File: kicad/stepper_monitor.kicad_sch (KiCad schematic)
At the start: 59 parts, among them J1 Conn_01x04_Pin, J2 Conn_01x04_Pin, J3 Conn_01x02_Pin, J4 USB_C_Receptacle_USB2.0, J5 JTAG, M1 Motor-simple_stepper_motor_an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, Q1 MMDT2222A, SW1 SW_Push, U1 5V, U2 CP2102N-A01-GQFN28, U3 AMS1117-3.3, U4 CC6920BSO-5A, U5 CC6920BSO-5A, U6 ESP32-WROOM-32U-N4

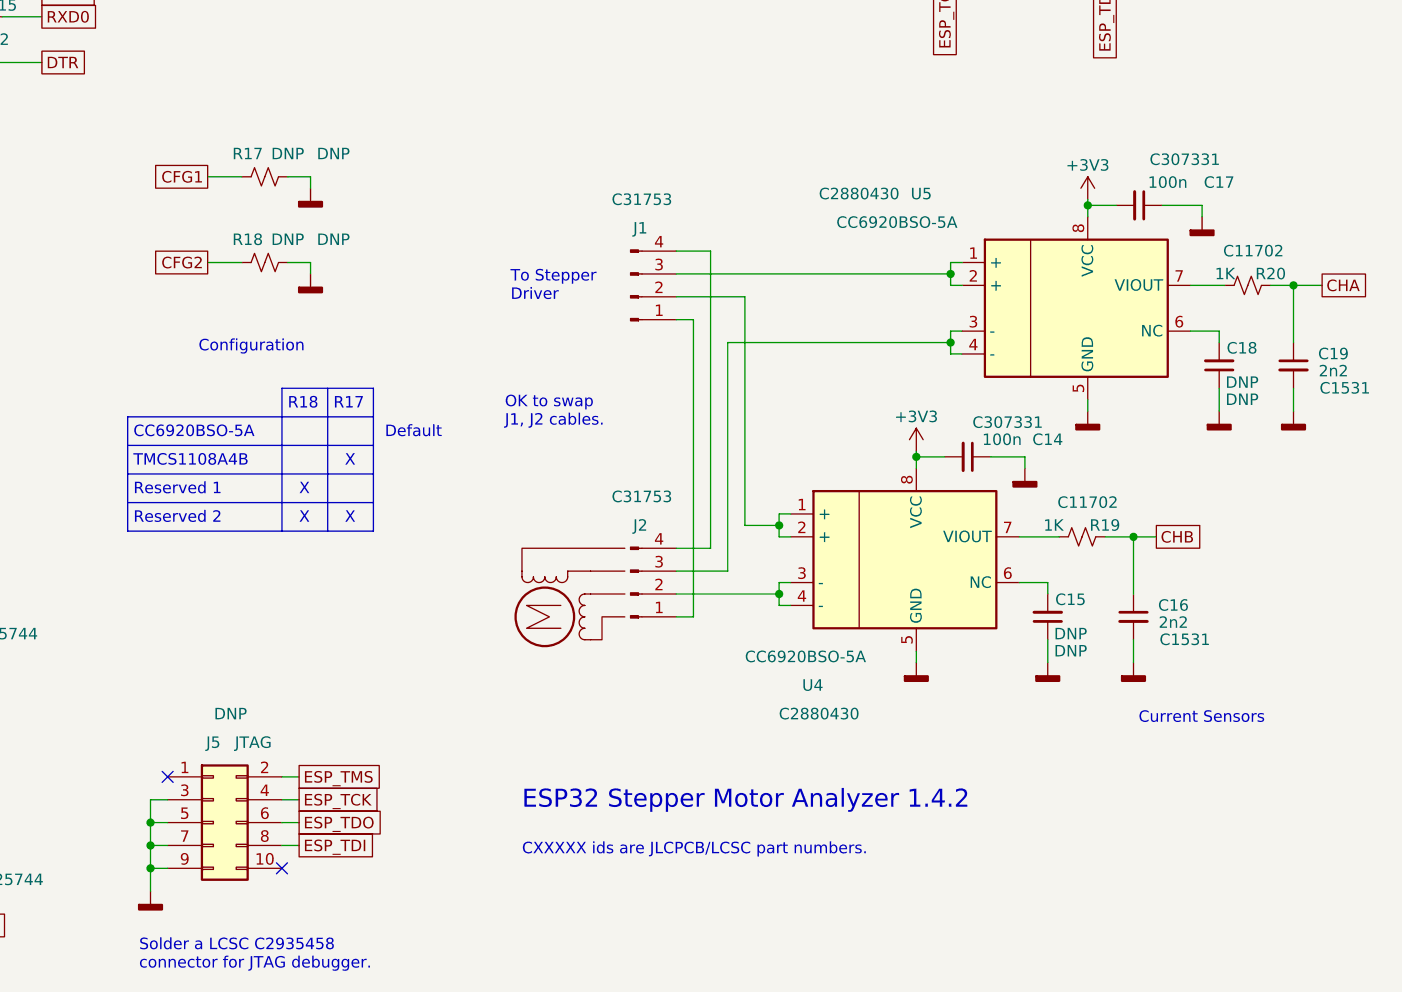
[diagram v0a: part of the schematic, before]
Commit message: Added 3D model for tactile switch.
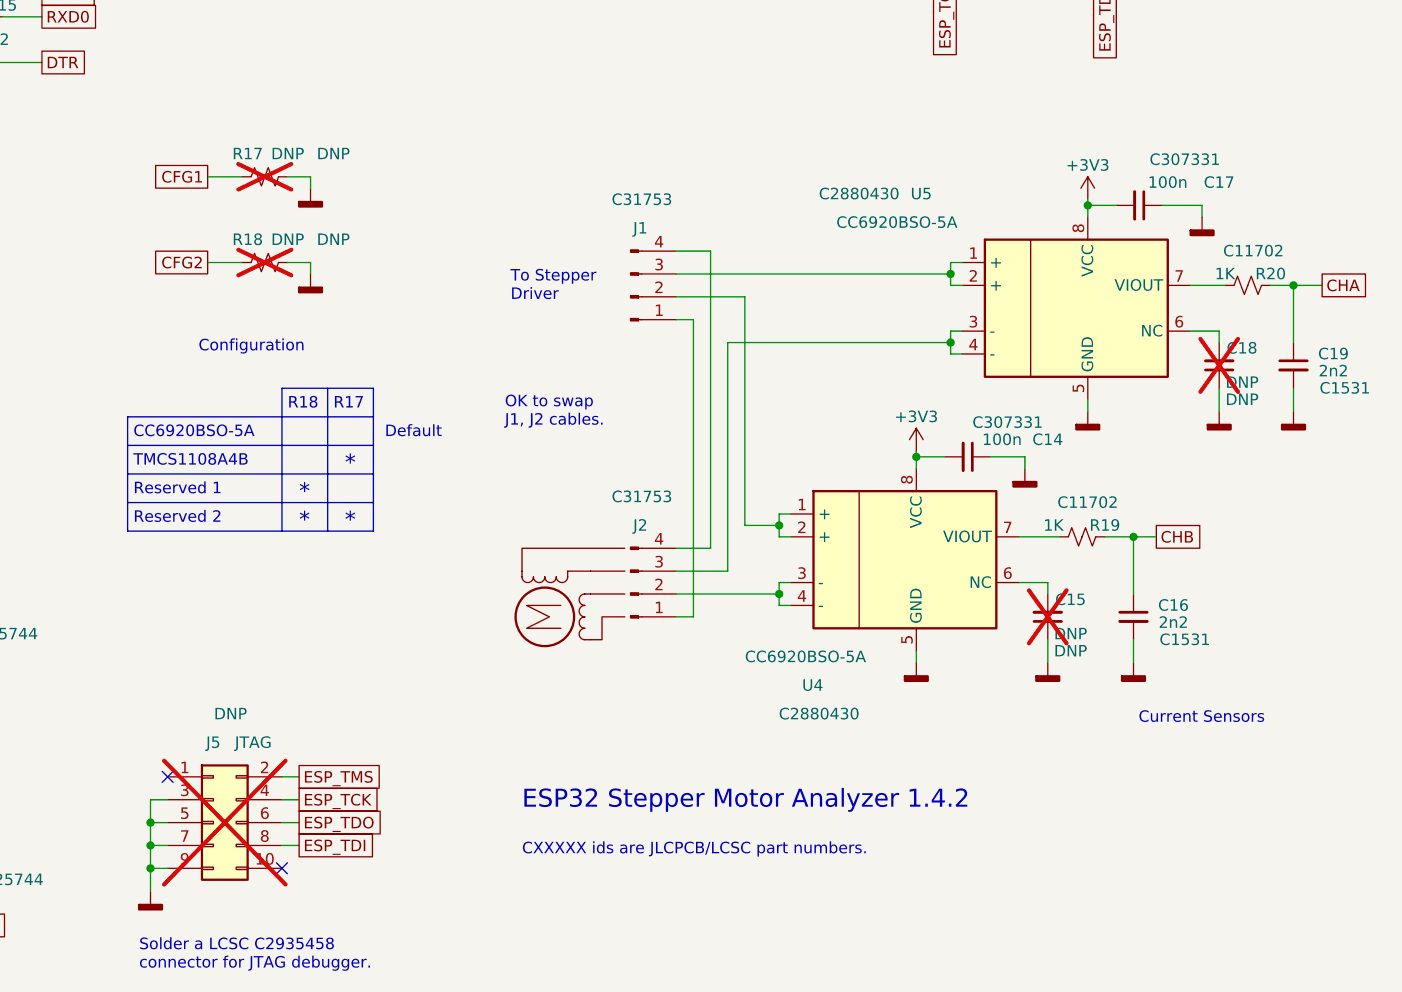
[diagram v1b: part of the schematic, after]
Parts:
- C15, C18, J5, R17, R18: now not fitted
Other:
- note added: "*"
- note removed: "X"
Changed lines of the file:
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@@
     (effects (font (size 1.27 1.27)) (justify right bottom))
-  )
-  (text "X" (at 164.465 135.255 0)
-    (effects (font (size 1.27 1.27)) (justify left bottom))
   )
   (text "Reserved 2" (at 140.97 141.605 0)
@@
     (effects (font (size 1.27 1.27)) (justify left bottom))
   )
-  (text "X" (at 159.385 138.43 0)
-    (effects (font (size 1.27 1.27)) (justify left bottom))
+  (text "*" (at 159.385 139.065 0)
+    (effects (font (size 1.778 1.778)) (justify left bottom))
   )
   (text "Configuration" (at 160.02 122.555 0)
@@
     (effects (font (size 1.27 1.27)) (justify left bottom))
   )
+  (text "*" (at 164.465 135.89 0)
+    (effects (font (size 1.778 1.778)) (justify left bottom))
+  )
+  (text "*" (at 164.465 142.24 0)
+    (effects (font (size 1.778 1.778)) (justify left bottom))
+  )
   (text "Reset Control" (at 101.6 191.135 0)
     (effects (font (size 1.27 1.27)) (justify right bottom))
@@
     (effects (font (size 1.27 1.27)) (justify left bottom))
   )
-  (text "X" (at 159.385 141.605 0)
-    (effects (font (size 1.27 1.27)) (justify left bottom))
-  )
   (text "CC6920BSO-5A" (at 140.97 132.08 0)
     (effects (font (size 1.27 1.27)) (justify left bottom))
@@
     (effects (font (size 1.27 1.27)) (justify left bottom))
   )
-  (text "X" (at 164.465 141.605 0)
-    (effects (font (size 1.27 1.27)) (justify left bottom))
-  )
   (text "MCU + BLE" (at 222.25 78.105 0)
     (effects (font (size 1.27 1.27)) (justify right bottom))
@@
   (text "Power supply" (at 90.17 57.785 0)
     (effects (font (size 1.27 1.27)) (justify right bottom))
+  )
+  (text "*" (at 159.385 142.24 0)
+    (effects (font (size 1.778 1.778)) (justify left bottom))
   )
   (text "ESP32 Stepper Motor Analyzer 1.4.2" (at 184.15 173.355 0)
@@
   )
   (symbol (lib_id "Device:R_Small_US") (at 155.575 112.395 90) (unit 1)
-    (in_bom yes) (on_board yes) (dnp no)
+    (in_bom yes) (on_board yes) (dnp yes)
     (property "Reference" "R18" (at 153.67 109.855 90)
       (effects (font (size 1.27 1.27)))
@@
   )
   (symbol (lib_id "Device:C_Small") (at 242.57 151.765 180) (unit 1)
-    (in_bom yes) (on_board yes) (dnp no)
+    (in_bom yes) (on_board yes) (dnp yes)
     (property "Reference" "C15" (at 245.11 149.86 0)
       (effects (font (size 1.27 1.27)))
@@
   )
   (symbol (lib_id "Connector_Generic:Conn_02x05_Odd_Even") (at 149.86 174.625 0) (unit 1)
-    (in_bom yes) (on_board yes) (dnp no)
+    (in_bom yes) (on_board yes) (dnp yes)
     (property "Reference" "J5" (at 149.86 165.735 0)
       (effects (font (size 1.27 1.27)))
@@
   )
   (symbol (lib_id "Device:C_Small") (at 261.62 123.825 180) (unit 1)
-    (in_bom yes) (on_board yes) (dnp no)
+    (in_bom yes) (on_board yes) (dnp yes)
     (property "Reference" "C18" (at 264.16 121.92 0)
       (effects (font (size 1.27 1.27)))
@@
   )
   (symbol (lib_id "Device:R_Small_US") (at 155.575 102.87 90) (unit 1)
-    (in_bom yes) (on_board yes) (dnp no)
+    (in_bom yes) (on_board yes) (dnp yes)
     (property "Reference" "R17" (at 153.67 100.33 90)
       (effects (font (size 1.27 1.27)))

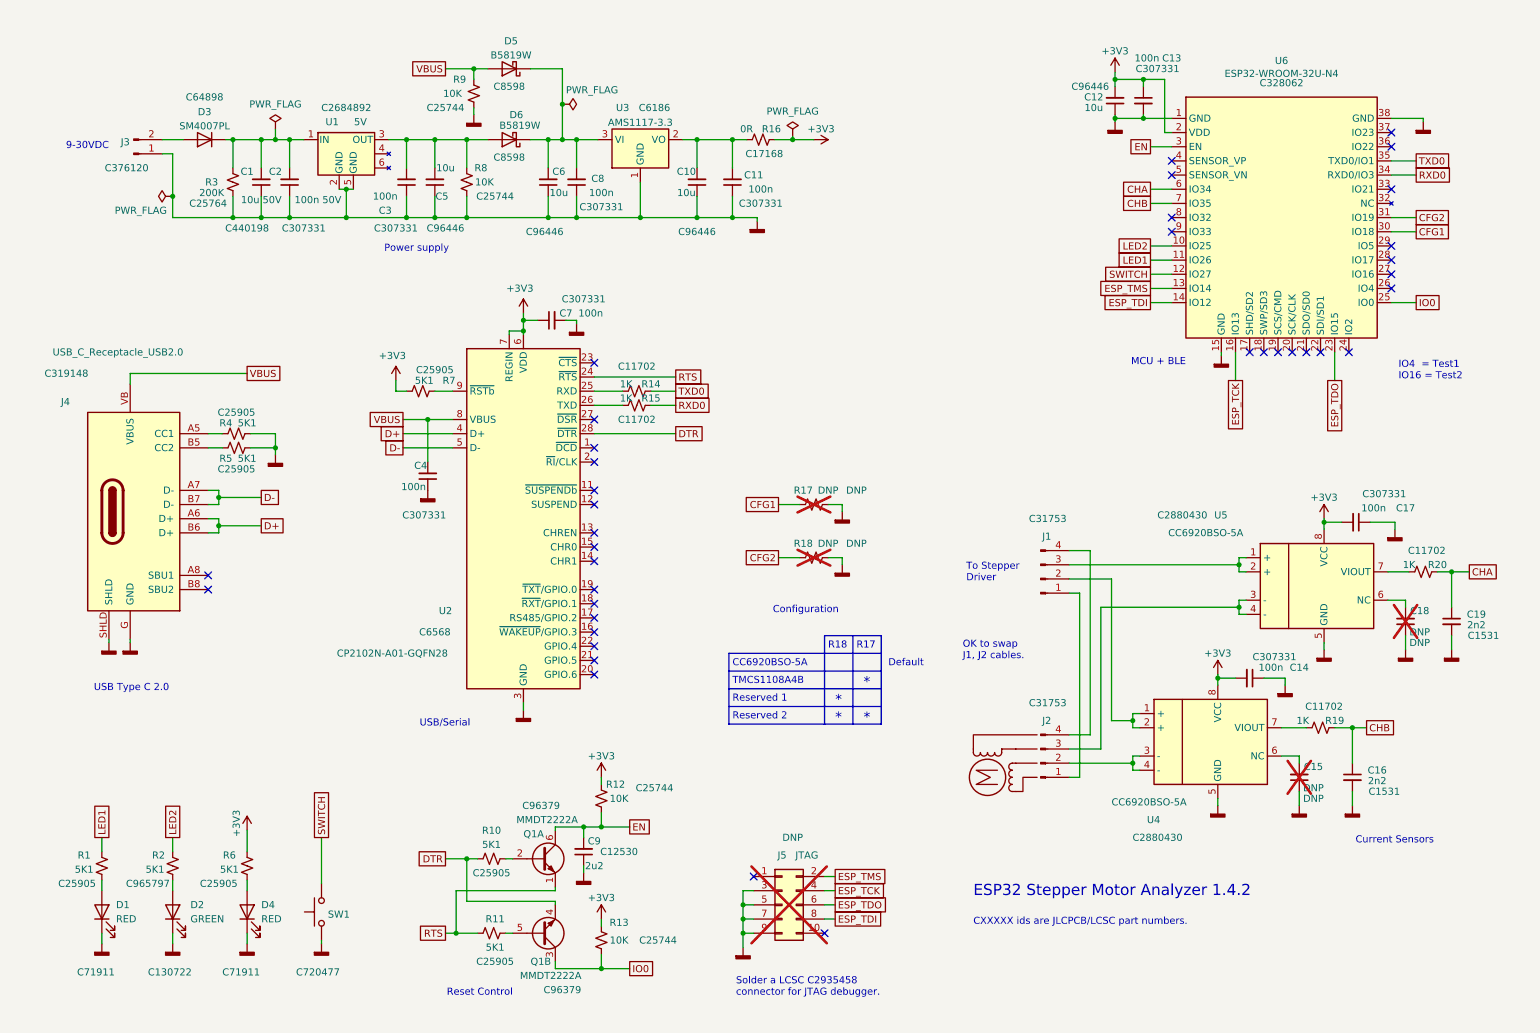
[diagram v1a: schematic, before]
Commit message: V3D Edition Design
- M3 corner holes
- JST XH connectors
- Match JLCPCB capabilities
- increased board size
- increased via size
- adjusted tracks in some locations to match capabilities
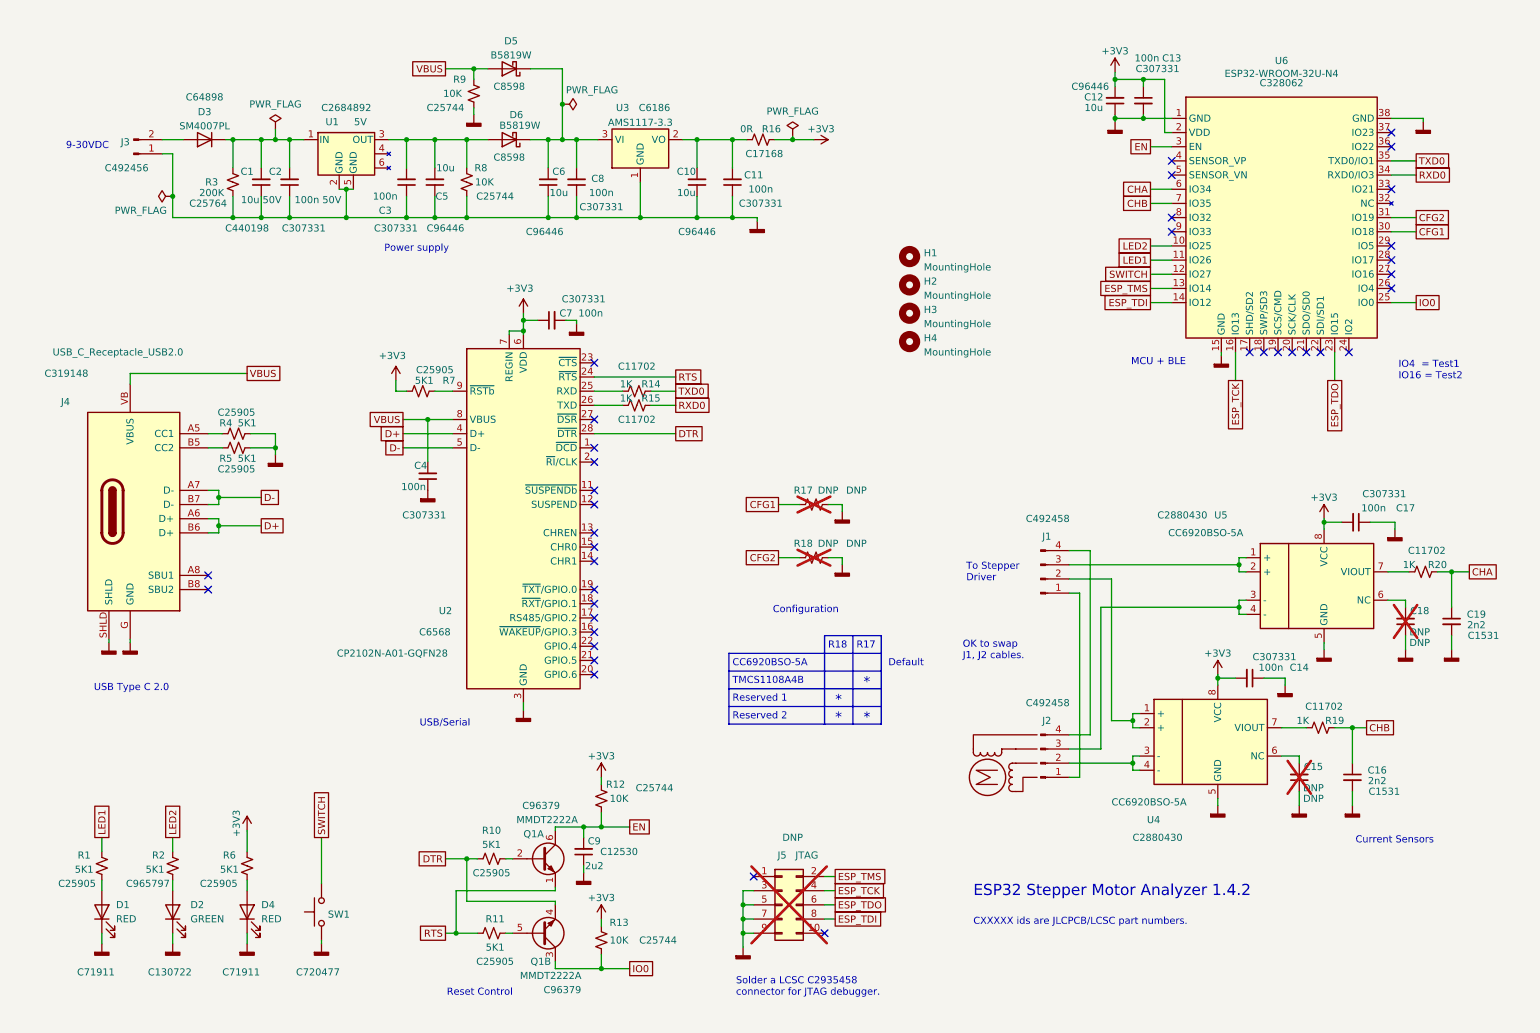
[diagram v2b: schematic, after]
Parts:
- added H1, H2, H3, H4: MountingHole, MountingHole:MountingHole_3.2mm_M3_Pad_Via, symbol Mechanical:MountingHole
- J1, J2: footprint stepper_monitor:connector_4pins_horizontal -> Connector_JST:JST_XH_B4B-XH-A_1x04_P2.50mm_Vertical; LCSC C31753 -> C492458
- J3: footprint stepper_monitor:PinHeader_1x02_P2.54mm_Horizontal_JLCPCB -> Connector_JST:JST_XH_B2B-XH-A_1x02_P2.50mm_Vertical; LCSC C376120 -> C492456
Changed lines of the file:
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@@
       (effects (font (size 1.27 1.27)) (justify right) hide)
     )
-    (property "Footprint" "stepper_monitor:PinHeader_1x02_P2.54mm_Horizontal_JLCPCB" (at 33.655 40.005 0)
+    (property "Footprint" "Connector_JST:JST_XH_B2B-XH-A_1x02_P2.50mm_Vertical" (at 33.655 40.005 0)
       (effects (font (size 1.27 1.27)) hide)
     )
@@
       (effects (font (size 1.27 1.27)) hide)
     )
-    (property "LCSC" "C376120" (at 32.385 42.545 0)
+    (property "LCSC" "C492456" (at 32.385 42.545 0)
       (effects (font (size 1.27 1.27)))
     )
@@
       (effects (font (size 1.27 1.27)) (justify right) hide)
     )
-    (property "Footprint" "stepper_monitor:connector_4pins_horizontal" (at 196.215 149.225 0)
+    (property "Footprint" "Connector_JST:JST_XH_B4B-XH-A_1x04_P2.50mm_Vertical" (at 196.215 149.225 0)
       (effects (font (size 1.27 1.27)) hide)
     )
@@
       (effects (font (size 1.27 1.27)) hide)
     )
-    (property "LCSC" "C31753" (at 197.485 138.43 0)
+    (property "LCSC" "C492458" (at 197.485 138.43 0)
       (effects (font (size 1.27 1.27)))
     )
@@
         (path "/ab9a1617-734a-47a3-94aa-b13da0ec18df"
           (reference "#PWR028") (unit 1)
+        )
+      )
+    )
+  )
+  (symbol (lib_id "Mechanical:MountingHole") (at 172.72 73.66 0) (unit 1)
+    (in_bom yes) (on_board yes) (dnp no) (fields_autoplaced)
+    (property "Reference" "H4" (at 175.26 73.025 0)
+      (effects (font (size 1.27 1.27)) (justify left))
+    )
+    (property "Value" "MountingHole" (at 175.26 75.565 0)
+      (effects (font (size 1.27 1.27)) (justify left))
+    )
+    (property "Footprint" "MountingHole:MountingHole_3.2mm_M3_Pad_Via" (at 172.72 73.66 0)
+      (effects (font (size 1.27 1.27)) hide)
+    )
+    (property "Datasheet" "~" (at 172.72 73.66 0)
+      (effects (font (size 1.27 1.27)) hide)
+    )
+    (instances
+      (project "stepper_monitor"
+        (path "/ab9a1617-734a-47a3-94aa-b13da0ec18df"
+          (reference "H4") (unit 1)
+        )
+      )
+    )
+  )
+  (symbol (lib_id "Mechanical:MountingHole") (at 172.72 63.5 0) (unit 1)
+    (in_bom yes) (on_board yes) (dnp no) (fields_autoplaced)
+    (property "Reference" "H2" (at 175.26 62.865 0)
+      (effects (font (size 1.27 1.27)) (justify left))
+    )
+    (property "Value" "MountingHole" (at 175.26 65.405 0)
+      (effects (font (size 1.27 1.27)) (justify left))
+    )
+    (property "Footprint" "MountingHole:MountingHole_3.2mm_M3_Pad_Via" (at 172.72 63.5 0)
+      (effects (font (size 1.27 1.27)) hide)
+    )
+    (property "Datasheet" "~" (at 172.72 63.5 0)
+      (effects (font (size 1.27 1.27)) hide)
+    )
+    (instances
+      (project "stepper_monitor"
+        (path "/ab9a1617-734a-47a3-94aa-b13da0ec18df"
+          (reference "H2") (unit 1)
         )
       )
@@
     )
   )
+  (symbol (lib_id "Mechanical:MountingHole") (at 172.72 68.58 0) (unit 1)
+    (in_bom yes) (on_board yes) (dnp no) (fields_autoplaced)
+    (property "Reference" "H3" (at 175.26 67.945 0)
+      (effects (font (size 1.27 1.27)) (justify left))
+    )
+    (property "Value" "MountingHole" (at 175.26 70.485 0)
+      (effects (font (size 1.27 1.27)) (justify left))
+    )
+    (property "Footprint" "MountingHole:MountingHole_3.2mm_M3_Pad_Via" (at 172.72 68.58 0)
+      (effects (font (size 1.27 1.27)) hide)
+    )
+    (property "Datasheet" "~" (at 172.72 68.58 0)
+      (effects (font (size 1.27 1.27)) hide)
+    )
+    (instances
+      (project "stepper_monitor"
+        (path "/ab9a1617-734a-47a3-94aa-b13da0ec18df"
+          (reference "H3") (unit 1)
+        )
+      )
+    )
+  )
   (symbol (lib_id "Device:D_Schottky") (at 100.965 37.465 180) (unit 1)
     (in_bom yes) (on_board yes) (dnp no)
@@
       (effects (font (size 1.27 1.27)) (justify right) hide)
     )
-    (property "Footprint" "stepper_monitor:connector_4pins_horizontal" (at 196.215 116.205 0)
+    (property "Footprint" "Connector_JST:JST_XH_B4B-XH-A_1x04_P2.50mm_Vertical" (at 196.215 116.205 0)
       (effects (font (size 1.27 1.27)) hide)
     )
@@
       (effects (font (size 1.27 1.27)) hide)
     )
-    (property "LCSC" "C31753" (at 197.485 105.41 0)
+    (property "LCSC" "C492458" (at 197.485 105.41 0)
       (effects (font (size 1.27 1.27)))
     )
@@
         )
       )
+    )
+  )
+  (symbol (lib_id "Mechanical:MountingHole") (at 172.72 58.42 0) (unit 1)
+    (in_bom yes) (on_board yes) (dnp no) (fields_autoplaced)
+    (property "Reference" "H1" (at 175.26 57.785 0)
+      (effects (font (size 1.27 1.27)) (justify left))
+    )
+    (property "Value" "MountingHole" (at 175.26 60.325 0)
+      (effects (font (size 1.27 1.27)) (justify left))
+    )
+    (property "Footprint" "MountingHole:MountingHole_3.2mm_M3_Pad_Via" (at 172.72 58.42 0)
+      (effects (font (size 1.27 1.27)) hide)
+    )
+    (property "Datasheet" "~" (at 172.72 58.42 0)
+      (effects (font (size 1.27 1.27)) hide)
+    )
+    (instances
+      (project "stepper_monitor"
+        (path "/ab9a1617-734a-47a3-94aa-b13da0ec18df"
+          (reference "H1") (unit 1)
+        )
+      )
